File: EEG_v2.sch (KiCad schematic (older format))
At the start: 11 parts, among them P1 CONN_5X2, P2 CONN_1, P3 CONN_1, P4 USB_A, P5 CONN_8, P6 CONN_8, P7 CONN_3, SW1 SWITCH_INV, SW4 RESET

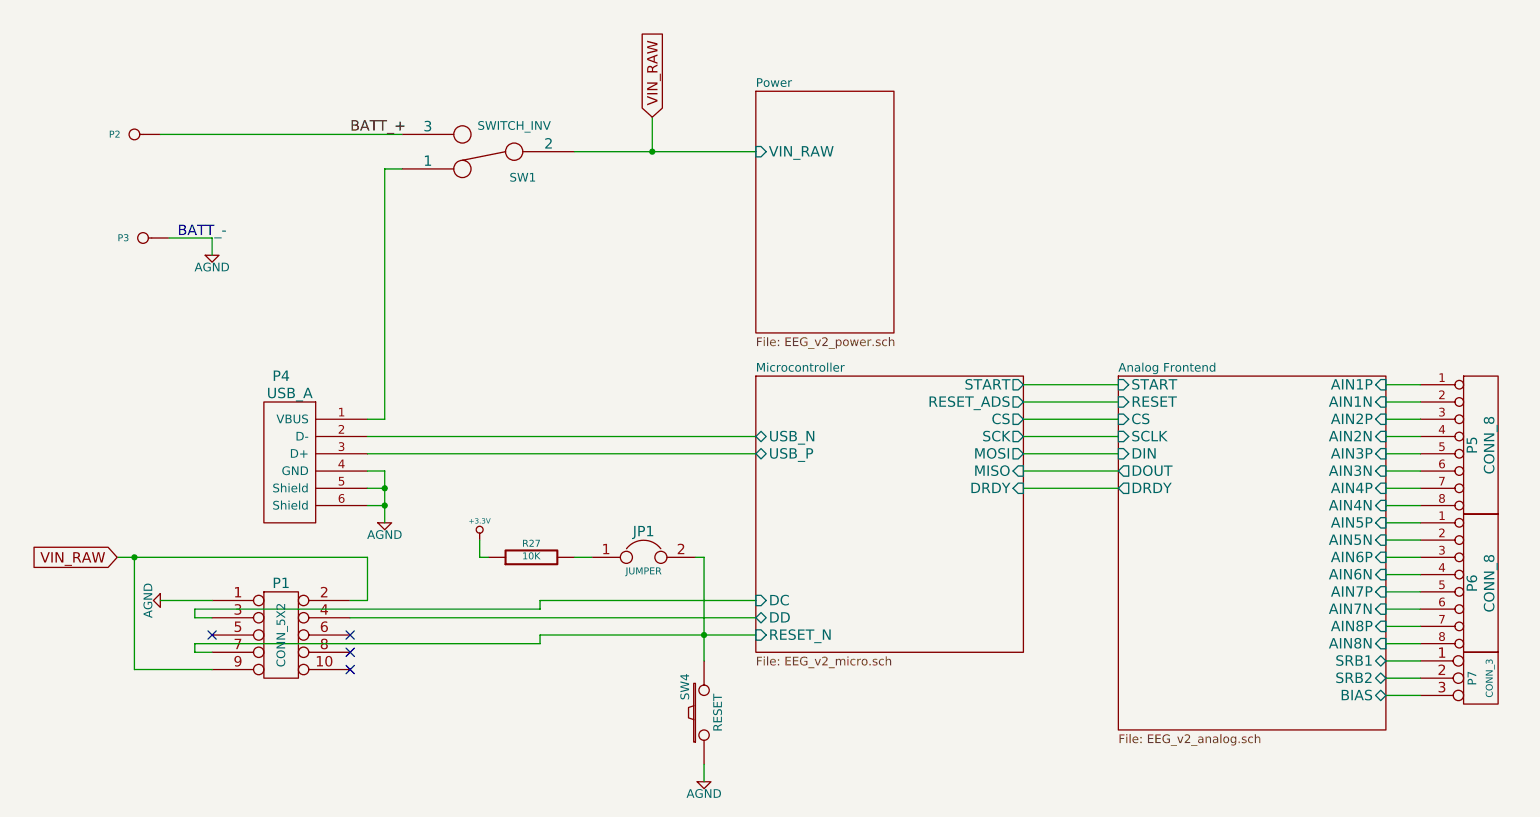
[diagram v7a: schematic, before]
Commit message: Added footprints to connectors. Changed usb A to usb micro B
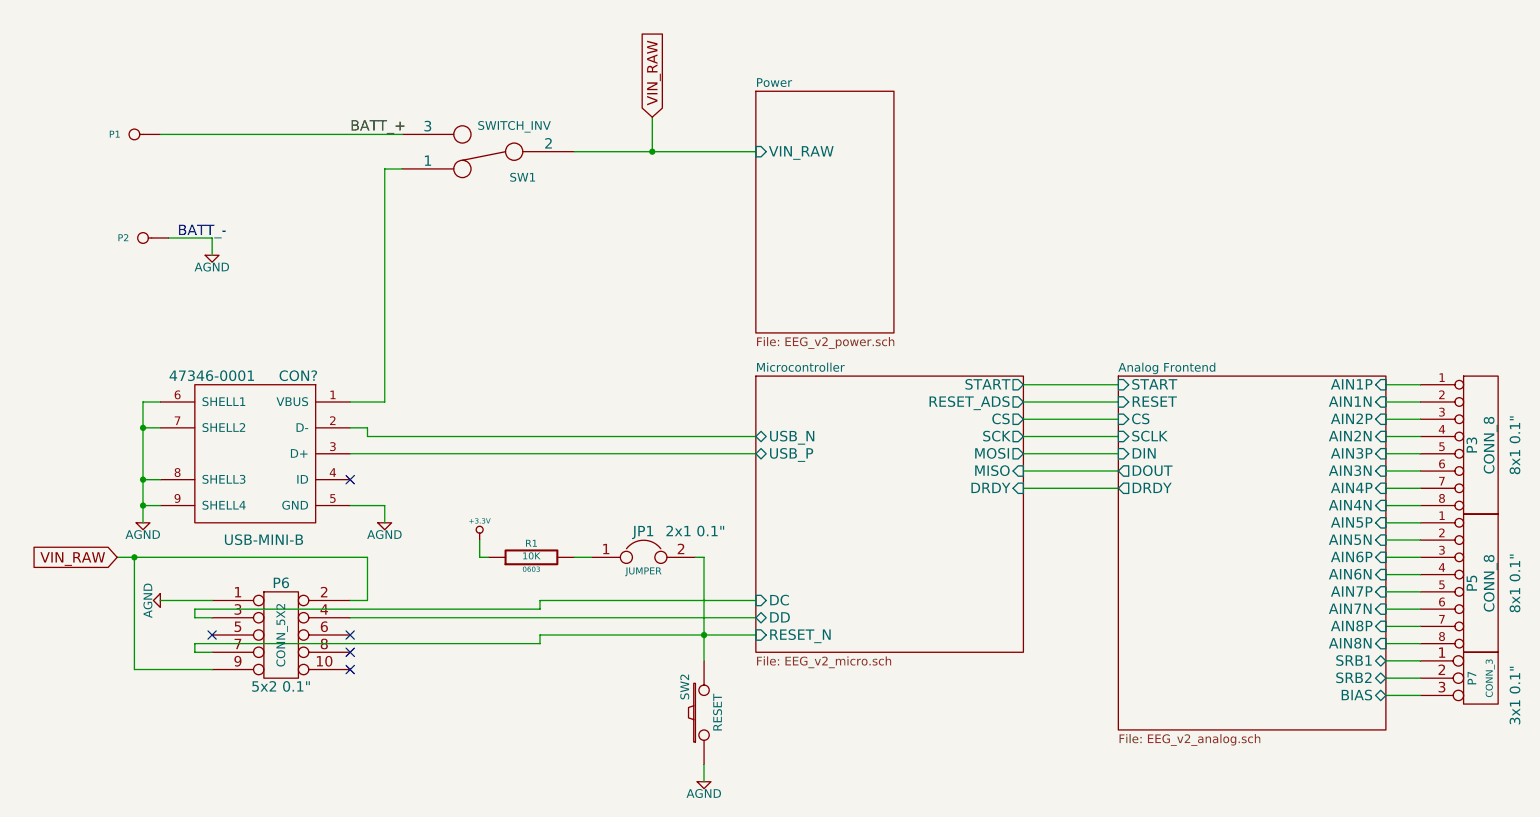
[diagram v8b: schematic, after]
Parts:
- removed P4: USB_A, symbol USB_A
- added CON?: USB-MINI-B, 47346-0001, symbol USB-MINI-B
- JP1: footprint ~ -> 2x1 0.1\"
- P3: renamed from P5; footprint ~ -> 8x1 0.1\"
- P5: renamed from P6; footprint ~ -> 8x1 0.1\"
- P6: renamed from P1; footprint ~ -> 5x2 0.1\"
- P7: footprint ~ -> 3x1 0.1\"
- R1: renamed from R27; footprint ~ -> 0603
- renumbered P2 to P1, P3 to P2, SW4 to SW2
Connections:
- net AGND: now also CON?.5 (GND), CON?.6 (SHELL1), CON?.7 (SHELL2), CON?.8 (SHELL3), CON?.9 (SHELL4)
- net Microcontroller/USB_N: now also CON?.2 (D-)
- net Microcontroller/USB_P: now also CON?.3 (D+)
- net at SW1.1: now also CON?.1 (VBUS)
- no-connect marks 4 -> 5
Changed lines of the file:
@@
 $EndSheet
-$Comp
-L USB_A P4
-U 1 1 54C36FB9
-P 2350 4700
-F 0 "P4" H 2150 5200 60  0000 C CNN
-F 1 "USB_A" H 2200 5100 60  0000 C CNN
-F 2 "" H 1900 4700 60  0000 C CNN
-F 3 "" H 1900 4700 60  0000 C CNN
-	1    2350 4700
-	1    0    0    -1
-$EndComp
-Wire Wire Line
-	6450 4250 7000 4250
-Wire Wire Line
-	7000 4350 6450 4350
-Wire Wire Line
-	6450 4450 7000 4450
-Wire Wire Line
-	7000 4550 6450 4550
-Wire Wire Line
-	6450 4650 7000 4650
-Wire Wire Line
-	7000 4750 6450 4750
-Wire Wire Line
-	6450 4850 7000 4850
-Wire Wire Line
-	4900 4550 2650 4550
-Wire Wire Line
-	2650 4650 4900 4650
-Wire Wire Line
-	2650 4750 2750 4750
-Wire Wire Line
-	2650 4850 2750 4850
-Connection ~ 2750 4850
-Wire Wire Line
-	2750 4950 2650 4950
-Connection ~ 2750 4950
 $Comp
 L AGND #PWR01
@@
 	1    0    0    -1
 $EndComp
-Wire Wire Line
-	3850 2900 4900 2900
-Connection ~ 4300 2900
-$Comp
-L CONN_1 P2
+$Comp
+L CONN_1 P1
 U 1 1 54C44DCA
 P 1300 2800
-F 0 "P2" H 1380 2800 40  0000 L CNN
+F 0 "P1" H 1380 2800 40  0000 L CNN
 F 1 "CONN_1" H 1300 2855 30  0001 C CNN
 F 2 "~" H 1300 2800 60  0000 C CNN
@@
 $EndComp
 $Comp
-L CONN_1 P3
+L CONN_1 P2
 U 1 1 54C44DD9
 P 1350 3400
-F 0 "P3" H 1430 3400 40  0000 L CNN
+F 0 "P2" H 1430 3400 40  0000 L CNN
 F 1 "CONN_1" H 1350 3455 30  0001 C CNN
 F 2 "~" H 1350 3400 60  0000 C CNN
@@
 	-1   0    0    1
 $EndComp
-Wire Wire Line
-	1450 2800 2850 2800
-Wire Wire Line
-	1500 3400 1750 3400
-Wire Wire Line
-	1750 3400 1750 3500
 $Comp
 L AGND #PWR02
@@
 Text Notes 1550 3400 0    60   ~ 0
 BATT_-
-Wire Wire Line
-	2550 5600 4900 5600
-$Comp
-L CONN_8 P5
+$Comp
+L CONN_8 P3
 U 1 1 54C84F21
 P 9100 4600
-F 0 "P5" V 9050 4600 60  0000 C CNN
+F 0 "P3" V 9050 4600 60  0000 C CNN
 F 1 "CONN_8" V 9150 4600 60  0000 C CNN
-F 2 "~" H 9100 4600 60  0000 C CNN
+F 2 "8x1 0.1\"" V 9300 4600 60  0000 C CNN
 F 3 "~" H 9100 4600 60  0000 C CNN
 	1    9100 4600
@@
 $EndComp
 $Comp
-L CONN_8 P6
+L CONN_8 P5
 U 1 1 54C84F2E
 P 9100 5400
-F 0 "P6" V 9050 5400 60  0000 C CNN
+F 0 "P5" V 9050 5400 60  0000 C CNN
 F 1 "CONN_8" V 9150 5400 60  0000 C CNN
-F 2 "~" H 9100 5400 60  0000 C CNN
+F 2 "8x1 0.1\"" V 9300 5400 60  0000 C CNN
 F 3 "~" H 9100 5400 60  0000 C CNN
 	1    9100 5400
@@
 F 0 "P7" V 9050 5950 50  0000 C CNN
 F 1 "CONN_3" V 9150 5950 40  0000 C CNN
-F 2 "~" H 9100 5950 60  0000 C CNN
+F 2 "3x1 0.1\"" V 9300 5850 60  0000 C CNN
 F 3 "~" H 9100 5950 60  0000 C CNN
 	1    9100 5950
 	1    0    0    -1
 $EndComp
-Wire Wire Line
-	8550 4250 8750 4250
-Wire Wire Line
-	8750 4350 8550 4350
-Wire Wire Line
-	8550 4450 8750 4450
-Wire Wire Line
-	8750 4550 8550 4550
-Wire Wire Line
-	8550 4650 8750 4650
-Wire Wire Line
-	8750 4750 8550 4750
-Wire Wire Line
-	8550 4850 8750 4850
-Wire Wire Line
-	8750 4950 8550 4950
-Wire Wire Line
-	8550 5050 8750 5050
-Wire Wire Line
-	8750 5150 8550 5150
-Wire Wire Line
-	8550 5250 8750 5250
-Wire Wire Line
-	8750 5350 8550 5350
-Wire Wire Line
-	8550 5450 8750 5450
-Wire Wire Line
-	8750 5550 8550 5550
-Wire Wire Line
-	8550 5650 8750 5650
-Wire Wire Line
-	8750 5750 8550 5750
-Wire Wire Line
-	8550 5850 8750 5850
-Wire Wire Line
-	8750 5950 8550 5950
-Wire Wire Line
-	8550 6050 8750 6050
-$Comp
-L CONN_5X2 P1
+$Comp
+L CONN_5X2 P6
 U 1 1 54C8BF12
 P 2150 5700
-F 0 "P1" H 2150 6000 60  0000 C CNN
+F 0 "P6" H 2150 6000 60  0000 C CNN
 F 1 "CONN_5X2" V 2150 5700 50  0000 C CNN
-F 2 "~" H 2150 5700 60  0000 C CNN
+F 2 "5x2 0.1\"" H 2150 5400 60  0000 C CNN
 F 3 "~" H 2150 5700 60  0000 C CNN
 	1    2150 5700
 	1    0    0    -1
 $EndComp
-Wire Wire Line
-	2750 4750 2750 5050
 $Comp
 L AGND #PWR03
@@
 	0    1    1    0
 $EndComp
-Wire Wire Line
-	1650 5550 3650 5550
-Wire Wire Line
-	1650 5550 1650 5600
-Wire Wire Line
-	1650 5600 1750 5600
-Wire Wire Line
-	3650 5550 3650 5500
-Wire Wire Line
-	3650 5500 4900 5500
-Wire Wire Line
-	2650 5500 2550 5500
-Wire Wire Line
-	2650 5250 2650 5500
-Wire Wire Line
-	1750 5500 1450 5500
-Wire Wire Line
-	3650 5700 3650 5750
-Wire Wire Line
-	3650 5750 1650 5750
-Wire Wire Line
-	1650 5750 1650 5800
-Wire Wire Line
-	1650 5800 1750 5800
-Wire Wire Line
-	1300 5900 1750 5900
 NoConn ~ 2550 5700
 NoConn ~ 2550 5800
@@
 Text GLabel 1200 5250 0    60   Input ~ 0
 VIN_RAW
-Wire Wire Line
-	1300 5900 1300 5250
-Wire Wire Line
-	1200 5250 2650 5250
-Connection ~ 1300 5250
-Wire Wire Line
-	4300 2700 4300 2900
-Wire Wire Line
-	2650 4450 2750 4450
-Wire Wire Line
-	2750 4450 2750 3000
-Wire Wire Line
-	2750 3000 2850 3000
 $Comp
 L SWITCH_INV SW1
@@
 $EndComp
 $Comp
-L R R27
+L R R1
 U 1 1 54CA2962
 P 3600 5250
-F 0 "R27" V 3680 5250 40  0000 C CNN
+F 0 "R1" V 3680 5250 40  0000 C CNN
 F 1 "10K" V 3607 5251 40  0000 C CNN
-F 2 "~" V 3530 5250 30  0000 C CNN
+F 2 "0603" V 3530 5250 30  0000 C CNN
 F 3 "~" H 3600 5250 30  0000 C CNN
 	1    3600 5250
@@
 	1    0    0    -1
 $EndComp
-Wire Wire Line
-	4600 5250 4600 5850
-Connection ~ 4600 5700
-Wire Wire Line
-	3650 5700 4900 5700
 $Comp
 L JUMPER JP1
@@
 F 0 "JP1" H 4250 5400 60  0000 C CNN
 F 1 "JUMPER" H 4250 5170 40  0000 C CNN
-F 2 "~" H 4250 5250 60  0000 C CNN
+F 2 "2x1 0.1\"" H 4550 5400 60  0000 C CNN
 F 3 "~" H 4250 5250 60  0000 C CNN
 	1    4250 5250
 	1    0    0    -1
 $EndComp
-Wire Wire Line
-	3300 5150 3300 5250
-Wire Wire Line
-	3300 5250 3350 5250
-Wire Wire Line
-	4600 5250 4550 5250
-Wire Wire Line
-	3950 5250 3850 5250
-$Comp
-L SW_PUSH SW4
+$Comp
+L SW_PUSH SW2
 U 1 1 54CABD6B
 P 4600 6150
-F 0 "SW4" H 4750 6260 50  0000 C CNN
+F 0 "SW2" H 4750 6260 50  0000 C CNN
 F 1 "RESET" H 4600 6070 50  0000 C CNN
 F 2 "~" H 4600 6150 60  0000 C CNN
@@
 	1    0    0    -1
 $EndComp
+$Comp
+L USB-MINI-B CON?
+U 1 1 54CCBB99
+P 2000 4650
+F 0 "CON?" H 1750 5100 60  0000 C CNN
+F 1 "USB-MINI-B" H 1950 4150 60  0000 C CNN
+F 2 "47346-0001" H 2250 5100 60  0000 C CNN
+F 3 "~" H 2000 4650 60  0000 C CNN
+	1    2000 4650
+	-1   0    0    -1
+$EndComp
+$Comp
+L AGND #PWR?
+U 1 1 54CCD7A6
+P 1350 5050
+F 0 "#PWR?" H 1350 5050 40  0001 C CNN
+F 1 "AGND" H 1350 4980 50  0000 C CNN
+F 2 "~" H 1350 5050 60  0000 C CNN
+F 3 "~" H 1350 5050 60  0000 C CNN
+	1    1350 5050
+	1    0    0    -1
+$EndComp
+Wire Wire Line
+	6450 4250 7000 4250
+Wire Wire Line
+	7000 4350 6450 4350
+Wire Wire Line
+	6450 4450 7000 4450
+Wire Wire Line
+	7000 4550 6450 4550
+Wire Wire Line
+	6450 4650 7000 4650
+Wire Wire Line
+	7000 4750 6450 4750
+Wire Wire Line
+	6450 4850 7000 4850
+Wire Wire Line
+	4900 4550 2650 4550
+Wire Wire Line
+	2550 4650 4900 4650
+Wire Wire Line
+	2550 4950 2750 4950
+Wire Wire Line
+	3850 2900 4900 2900
+Connection ~ 4300 2900
+Wire Wire Line
+	1450 2800 2850 2800
+Wire Wire Line
+	1500 3400 1750 3400
+Wire Wire Line
+	1750 3400 1750 3500
+Wire Wire Line
+	2550 5600 4900 5600
+Wire Wire Line
+	8550 4250 8750 4250
+Wire Wire Line
+	8750 4350 8550 4350
+Wire Wire Line
+	8550 4450 8750 4450
+Wire Wire Line
+	8750 4550 8550 4550
+Wire Wire Line
+	8550 4650 8750 4650
+Wire Wire Line
+	8750 4750 8550 4750
+Wire Wire Line
+	8550 4850 8750 4850
+Wire Wire Line
+	8750 4950 8550 4950
+Wire Wire Line
+	8550 5050 8750 5050
+Wire Wire Line
+	8750 5150 8550 5150
+Wire Wire Line
+	8550 5250 8750 5250
+Wire Wire Line
+	8750 5350 8550 5350
+Wire Wire Line
+	8550 5450 8750 5450
+Wire Wire Line
+	8750 5550 8550 5550
+Wire Wire Line
+	8550 5650 8750 5650
+Wire Wire Line
+	8750 5750 8550 5750
+Wire Wire Line
+	8550 5850 8750 5850
+Wire Wire Line
+	8750 5950 8550 5950
+Wire Wire Line
+	8550 6050 8750 6050
+Wire Wire Line
+	1650 5550 3650 5550
+Wire Wire Line
+	1650 5550 1650 5600
+Wire Wire Line
+	1650 5600 1750 5600
+Wire Wire Line
+	3650 5550 3650 5500
+Wire Wire Line
+	3650 5500 4900 5500
+Wire Wire Line
+	2650 5500 2550 5500
+Wire Wire Line
+	2650 5250 2650 5500
+Wire Wire Line
+	1750 5500 1450 5500
+Wire Wire Line
+	3650 5700 3650 5750
+Wire Wire Line
+	3650 5750 1650 5750
+Wire Wire Line
+	1650 5750 1650 5800
+Wire Wire Line
+	1650 5800 1750 5800
+Wire Wire Line
+	1300 5900 1750 5900
+Wire Wire Line
+	1300 5900 1300 5250
+Wire Wire Line
+	1200 5250 2650 5250
+Connection ~ 1300 5250
+Wire Wire Line
+	4300 2700 4300 2900
+Wire Wire Line
+	2550 4350 2750 4350
+Wire Wire Line
+	2750 4350 2750 3000
+Wire Wire Line
+	2750 3000 2850 3000
+Wire Wire Line
+	4600 5250 4600 5850
+Connection ~ 4600 5700
+Wire Wire Line
+	3650 5700 4900 5700
+Wire Wire Line
+	3300 5150 3300 5250
+Wire Wire Line
+	3300 5250 3350 5250
+Wire Wire Line
+	4600 5250 4550 5250
+Wire Wire Line
+	3950 5250 3850 5250
 Wire Wire Line
 	4600 6450 4600 6550
+Wire Wire Line
+	2650 4550 2650 4500
+Wire Wire Line
+	2650 4500 2550 4500
+Wire Wire Line
+	2750 4950 2750 5050
+Wire Wire Line
+	1450 4950 1350 4950
+Wire Wire Line
+	1350 4350 1350 5050
+Wire Wire Line
+	1450 4350 1350 4350
+Connection ~ 1350 4950
+Wire Wire Line
+	1450 4500 1350 4500
+Connection ~ 1350 4500
+Wire Wire Line
+	1450 4800 1350 4800
+Connection ~ 1350 4800
+NoConn ~ 2550 4800
 $EndSCHEMATC
